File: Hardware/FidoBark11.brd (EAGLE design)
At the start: 40.3 x 45.7 mm, 25 parts, among them T1 BPX81, U1 MB85RC256VPF-G-JNERE2, U2 ADMP401

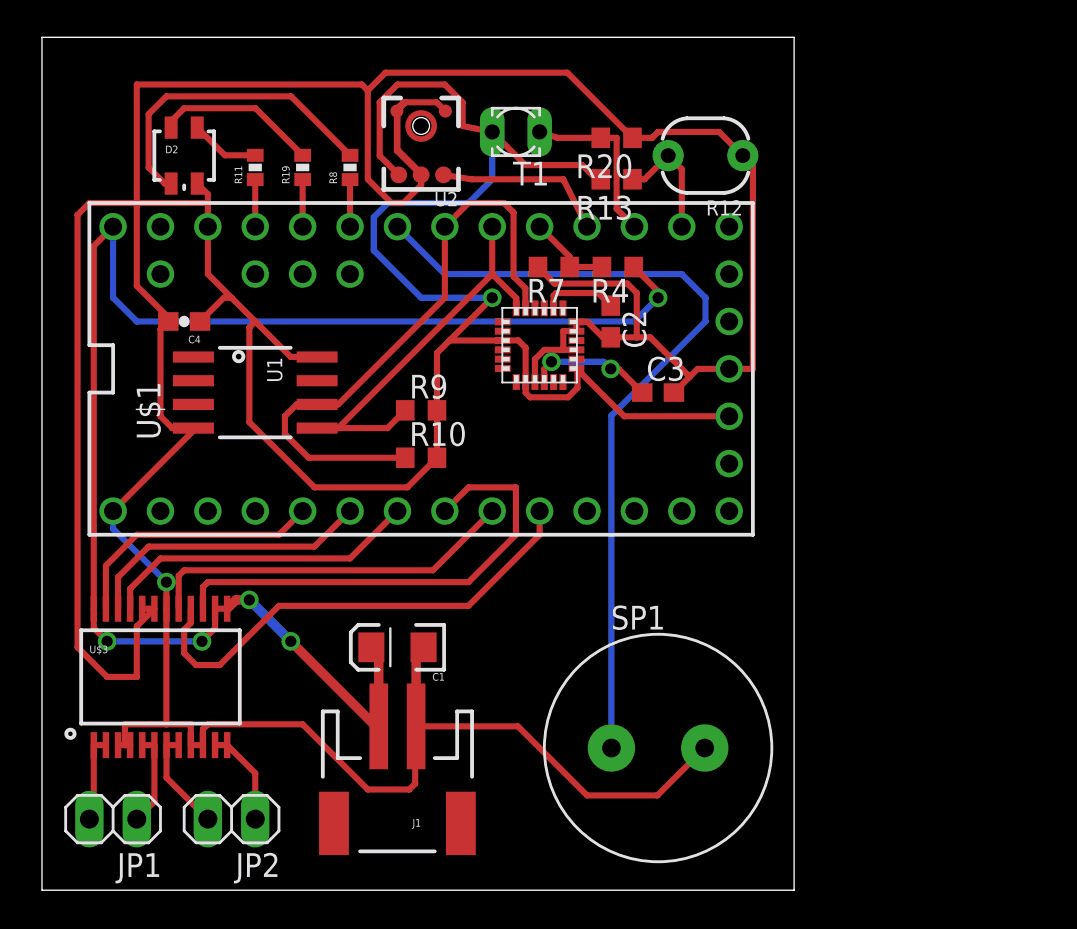
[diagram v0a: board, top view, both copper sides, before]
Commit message: mounting holes
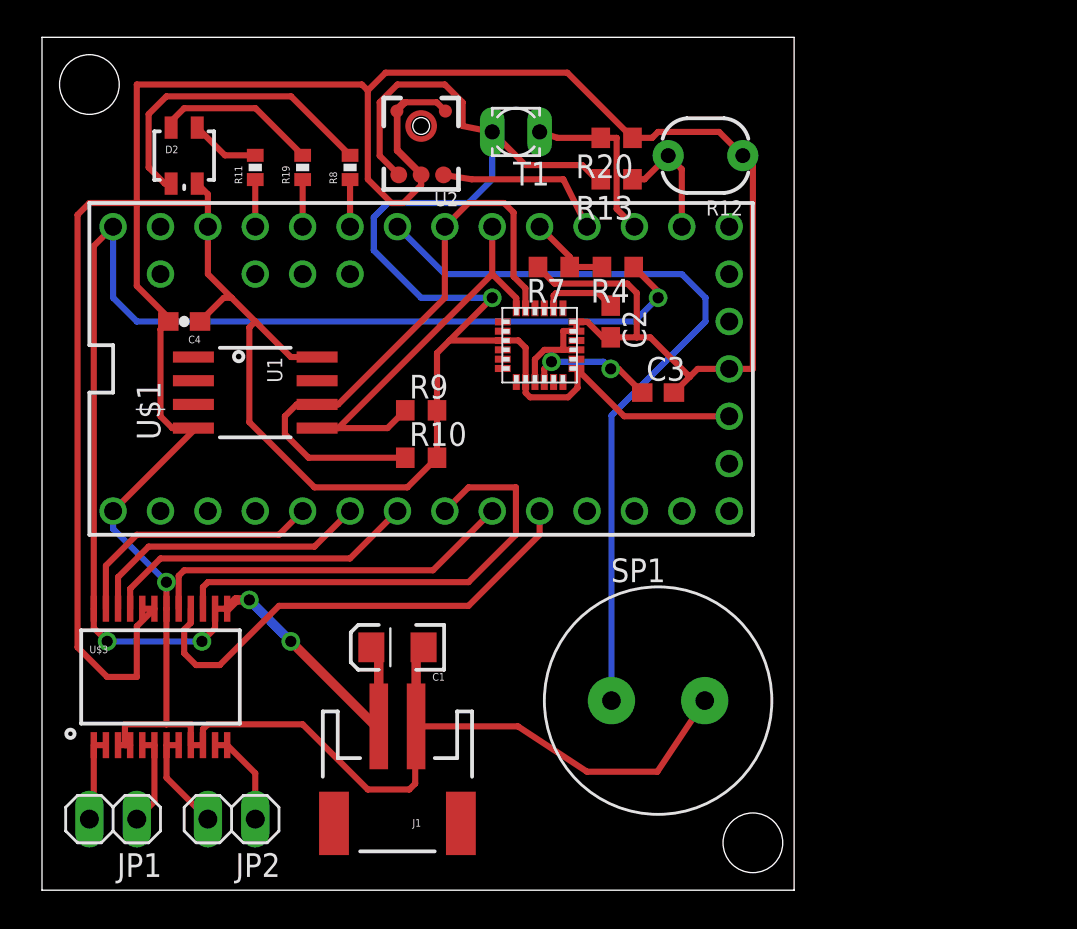
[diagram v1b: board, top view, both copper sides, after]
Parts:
- moved SP1 2.54 mm to (33.0, 10.2)
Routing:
- net PIEZO: track 44.3 -> 41.8 mm
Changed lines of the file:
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@@
 <layer number="43" name="vRestrict" color="2" fill="10" visible="yes" active="yes"/>
 <layer number="44" name="Drills" color="7" fill="1" visible="no" active="yes"/>
-<layer number="45" name="Holes" color="7" fill="1" visible="no" active="yes"/>
+<layer number="45" name="Holes" color="7" fill="1" visible="yes" active="yes"/>
 <layer number="46" name="Milling" color="3" fill="1" visible="no" active="yes"/>
 <layer number="47" name="Measures" color="7" fill="1" visible="no" active="yes"/>
@@
 <wire x1="40.31" y1="45.71" x2="0" y2="45.71" width="0" layer="20"/>
 <wire x1="0" y1="45.71" x2="0" y2="0" width="0" layer="20"/>
+<hole x="2.54" y="43.18" drill="3.2"/>
+<hole x="38.1" y="2.54" drill="3.2"/>
 </plain>
 <attributes>
@@
 <element name="R8" library="SparkFun" package="0402-RES" value="200" x="16.51" y="38.735" rot="R90"/>
 <element name="R9" library="rcl" package="R0603" value="10k" x="20.32" y="25.7175"/>
-<element name="SP1" library="adafruit" package="PS12" value="SPEAKER/PS12" x="33.02" y="7.62"/>
+<element name="SP1" library="adafruit" package="PS12" value="SPEAKER/PS12" x="33.02" y="10.16"/>
 <element name="T1" library="opto-trans-siemens" package="BPX81" value="BPX81" x="25.4" y="40.64" rot="R180">
 <attribute name="OC_NEWARK" value="unknown" x="25.4" y="40.64" size="1.778" layer="27" rot="R180" display="off"/>
@@
 <wire x1="20.0025" y1="8.7325" x2="20.05" y2="8.78" width="0.3302" layer="1"/>
 <wire x1="20.05" y1="8.78" x2="25.51" y2="8.78" width="0.3302" layer="1"/>
-<wire x1="25.51" y1="8.78" x2="29.21" y2="5.08" width="0.3302" layer="1"/>
-<wire x1="29.21" y1="5.08" x2="32.98" y2="5.08" width="0.3302" layer="1"/>
-<wire x1="32.98" y1="5.08" x2="35.52" y2="7.62" width="0.3302" layer="1"/>
+<wire x1="25.51" y1="8.78" x2="29.21" y2="6.35" width="0.3302" layer="1"/>
+<wire x1="29.21" y1="6.35" x2="32.98" y2="6.35" width="0.3302" layer="1"/>
+<wire x1="32.98" y1="6.35" x2="35.52" y2="10.16" width="0.3302" layer="1"/>
 <wire x1="20.45" y1="13.0175" x2="20.05" y2="12.6175" width="0.508" layer="1"/>
 <wire x1="20.05" y1="12.6175" x2="20.05" y2="8.78" width="0.508" layer="1"/>
@@
 <contactref element="SP1" pad="P$1"/>
 <contactref element="U$1" pad="20/A6"/>
-<wire x1="30.52" y1="7.62" x2="30.52" y2="25.44" width="0.3302" layer="16"/>
+<wire x1="30.52" y1="10.16" x2="30.52" y2="25.44" width="0.3302" layer="16"/>
 <wire x1="30.52" y1="25.44" x2="35.56" y2="30.48" width="0.3302" layer="16"/>
 <wire x1="35.56" y1="30.48" x2="35.56" y2="31.75" width="0.3302" layer="16"/>

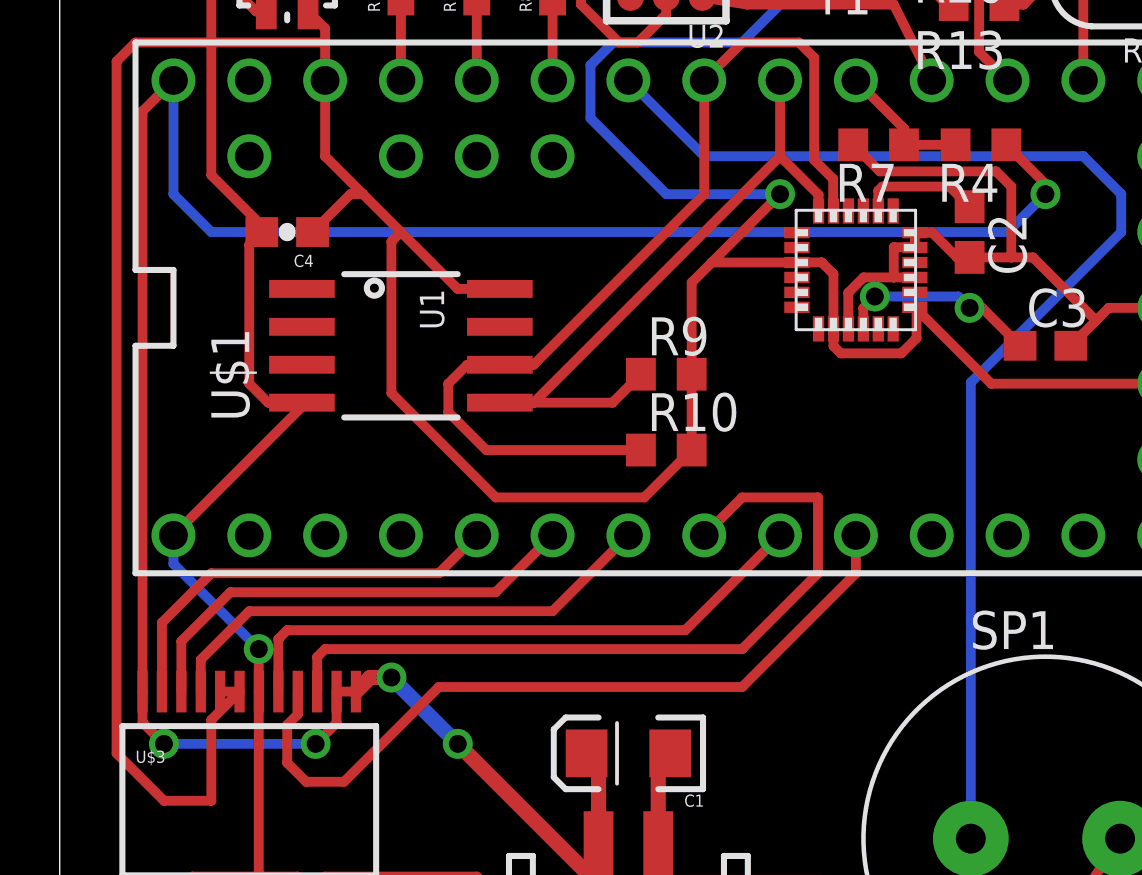
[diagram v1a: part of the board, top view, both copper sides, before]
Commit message: manufacturing tolerances compliance
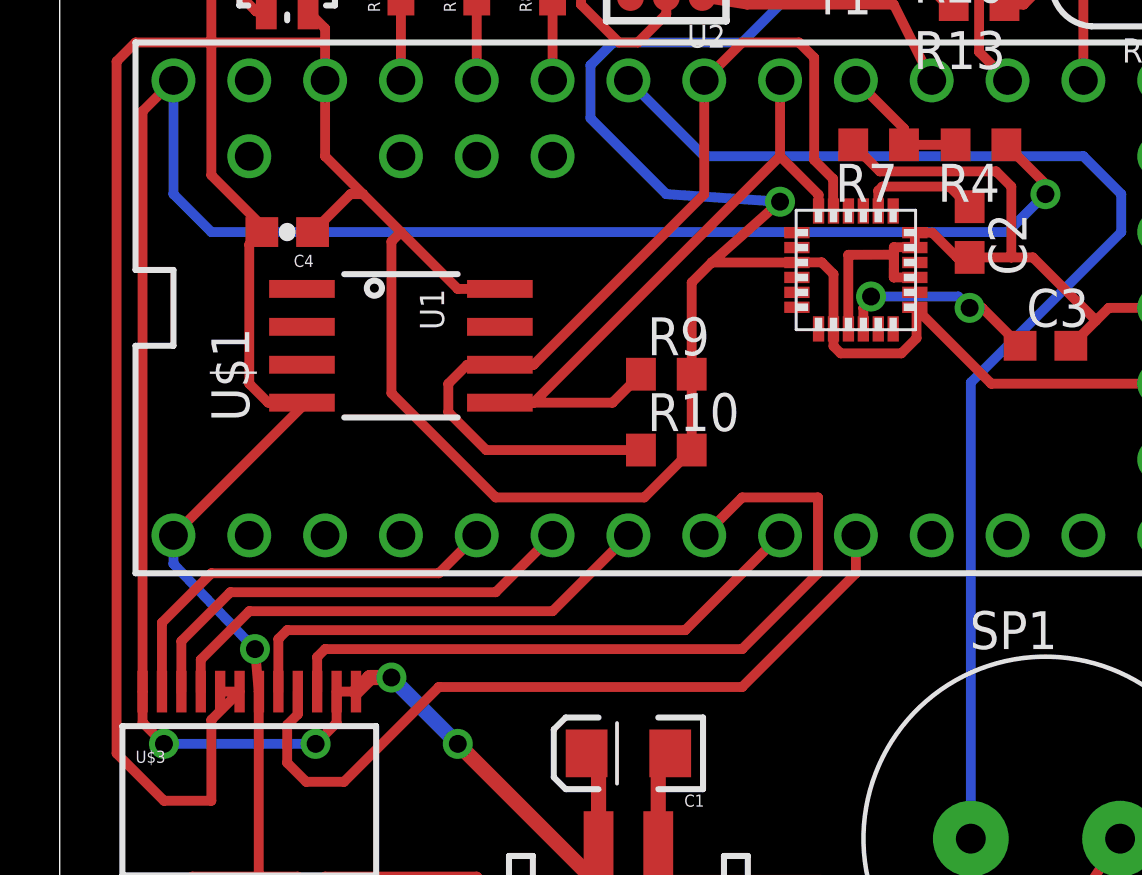
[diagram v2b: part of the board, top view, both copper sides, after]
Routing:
- net GND: track 180.2 -> 181.9 mm
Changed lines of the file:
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@@
 <wire x1="28.956" y1="38.862" x2="29.718" y2="38.1" width="0.3302" layer="1"/>
 <wire x1="29.718" y1="38.1" x2="29.9475" y2="38.1" width="0.3302" layer="1"/>
-<wire x1="21.84" y1="29.46" x2="24.13" y2="31.75" width="0.3302" layer="1"/>
-<via x="24.13" y="31.75" extent="1-16" drill="0.6" shape="square"/>
-<wire x1="24.13" y1="31.75" x2="20.32" y2="31.75" width="0.3302" layer="16"/>
+<wire x1="21.84" y1="29.46" x2="24.13" y2="31.496" width="0.3302" layer="1"/>
+<via x="24.13" y="31.496" extent="1-16" drill="0.6" shape="square"/>
+<wire x1="24.13" y1="31.496" x2="20.32" y2="31.75" width="0.3302" layer="16"/>
 <wire x1="20.32" y1="31.75" x2="17.78" y2="34.29" width="0.3302" layer="16"/>
 <wire x1="17.78" y1="34.29" x2="17.78" y2="36.068" width="0.3302" layer="16"/>
@@
 <wire x1="6.6675" y1="15.0785" x2="6.6675" y2="8.89" width="0.3302" layer="1"/>
 <wire x1="6.675" y1="15.086" x2="6.6675" y2="15.0935" width="0.3302" layer="1"/>
-<wire x1="6.6675" y1="15.0935" x2="6.6675" y2="16.51" width="0.3302" layer="1"/>
-<via x="6.6675" y="16.51" extent="1-16" drill="0.6" shape="square"/>
-<wire x1="6.6675" y1="16.51" x2="3.81" y2="19.3675" width="0.3302" layer="16"/>
+<wire x1="6.6675" y1="15.0935" x2="6.5405" y2="16.51" width="0.3302" layer="1"/>
+<via x="6.5405" y="16.51" extent="1-16" drill="0.6" shape="square"/>
+<wire x1="6.5405" y1="16.51" x2="3.81" y2="19.3675" width="0.3302" layer="16"/>
 <wire x1="3.81" y1="19.3675" x2="3.81" y2="20.32" width="0.3302" layer="16"/>
 <wire x1="8.625" y1="7.774" x2="8.625" y2="8.625" width="0.3302" layer="1"/>
@@
 <wire x1="6.985" y1="24.765" x2="8.115" y2="24.765" width="0.3302" layer="1"/>
 <wire x1="28.645" y1="28.96" x2="27.94" y2="28.96" width="0.3302" layer="1"/>
-<wire x1="27.94" y1="28.96" x2="26.928" y2="28.96" width="0.3302" layer="1"/>
-<wire x1="26.928" y1="28.96" x2="26.416" y2="28.448" width="0.3302" layer="1"/>
-<wire x1="26.416" y1="28.448" x2="26.416" y2="27.239" width="0.3302" layer="1"/>
+<wire x1="27.94" y1="28.96" x2="27.944" y2="29.722" width="0.3302" layer="1"/>
+<wire x1="27.944" y1="29.722" x2="26.416" y2="29.718" width="0.3302" layer="1"/>
+<wire x1="26.416" y1="29.718" x2="26.416" y2="27.239" width="0.3302" layer="1"/>
 <wire x1="26.416" y1="27.239" x2="26.42" y2="27.235" width="0.3302" layer="1"/>
 <wire x1="28.645" y1="30.46" x2="29.23" y2="30.46" width="0.3302" layer="1"/>
@@
 <via x="30.48" y="27.94" extent="1-16" drill="0.6" shape="square"/>
 <wire x1="30.48" y1="27.94" x2="30.099" y2="28.321" width="0.3302" layer="16"/>
-<wire x1="30.099" y1="28.321" x2="27.305" y2="28.321" width="0.3302" layer="16"/>
-<via x="27.305" y="28.321" extent="1-16" drill="0.6" shape="square"/>
-<wire x1="27.305" y1="28.321" x2="26.92" y2="27.936" width="0.3302" layer="1"/>
+<wire x1="30.099" y1="28.321" x2="27.178" y2="28.321" width="0.3302" layer="16"/>
+<via x="27.178" y="28.321" extent="1-16" drill="0.6" shape="square"/>
+<wire x1="27.178" y1="28.321" x2="26.92" y2="27.936" width="0.3302" layer="1"/>
 <wire x1="26.92" y1="27.936" x2="26.92" y2="27.235" width="0.3302" layer="1"/>
 </signal>
